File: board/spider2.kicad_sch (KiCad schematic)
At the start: 100 parts, among them J1 NRJ6HH, J10 PJ-320A, J11 PJ359, J12 PJ359, J13 PJ359, J14 PJ359, J15 PJ359, J16 PJ359, J19 PJ359, J2 NRJ6HH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

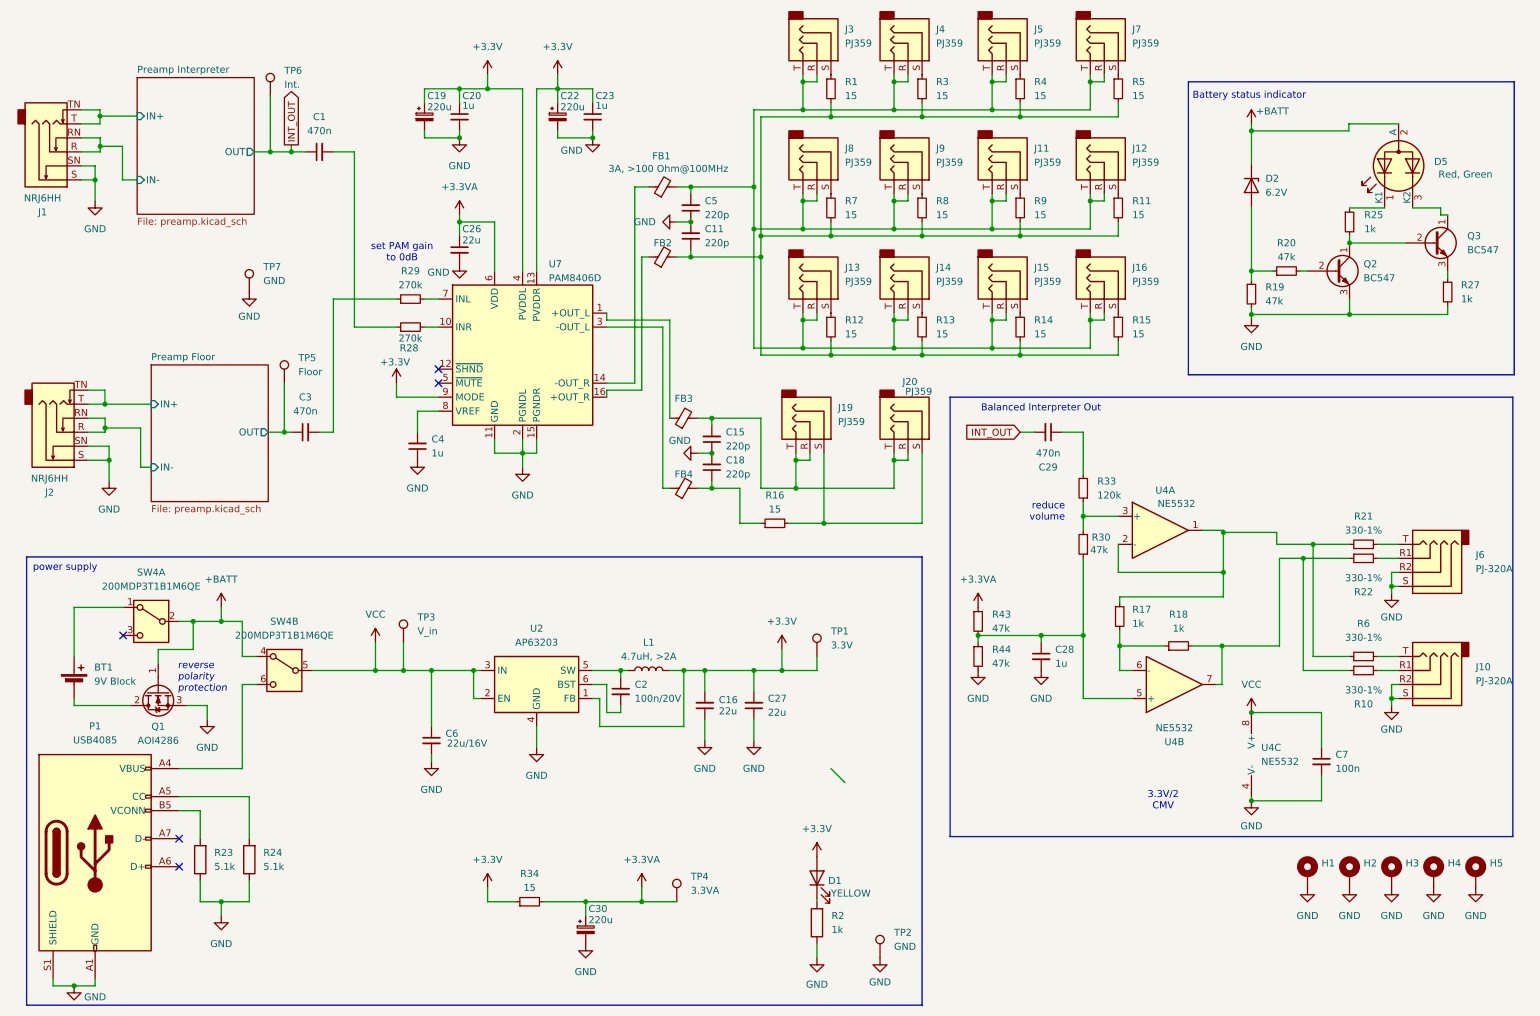
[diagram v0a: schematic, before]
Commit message: silkscreen updates
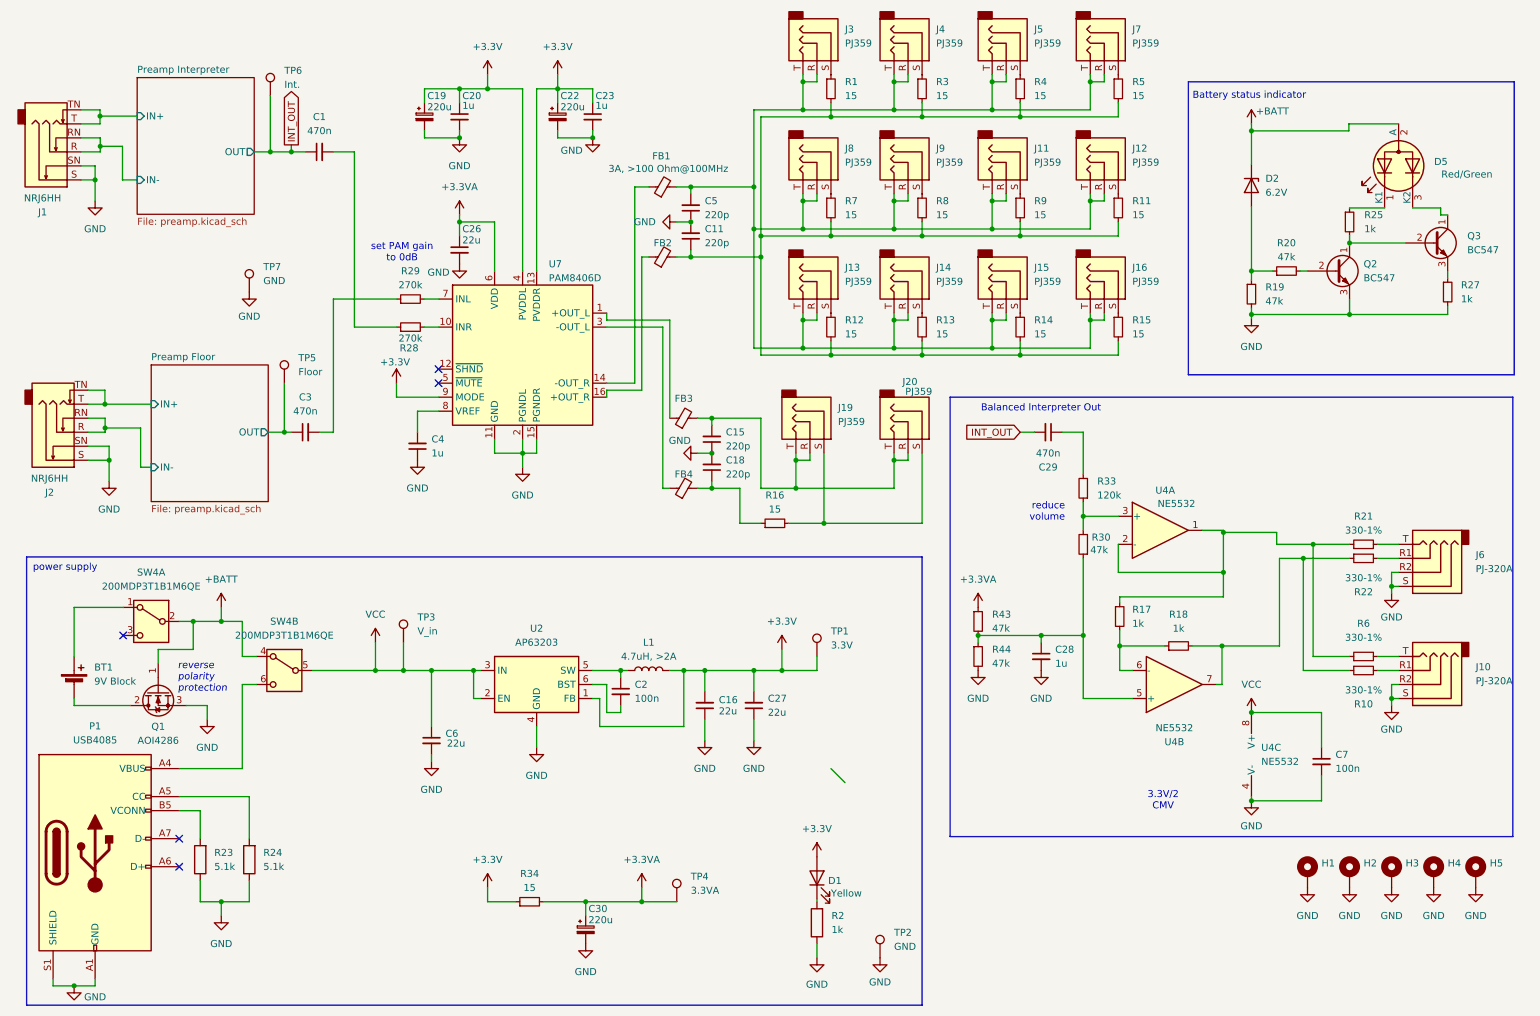
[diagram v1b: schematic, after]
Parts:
- C2: value 100n/20V -> 100n
- C6: value 22u/16V -> 22u
- D1: value YELLOW -> Yellow
- D5: value Red, Green -> Red/Green
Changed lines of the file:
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@@
 			)
 		)
-		(property "Value" "100n/20V"
+		(property "Value" "100n"
 			(at 124.46 139.7062 0)
 			(effects
@@
 			)
 		)
-		(property "Value" "YELLOW"
+		(property "Value" "Yellow"
 			(at 160.02 175.006 90)
 			(effects
@@
 			)
 		)
-		(property "Value" "22u/16V"
+		(property "Value" "22u"
 			(at 90.424 147.828 0)
 			(effects
@@
 			)
 		)
-		(property "Value" "Red, Green"
+		(property "Value" "Red/Green"
 			(at 279.908 44.704 90)
 			(effects

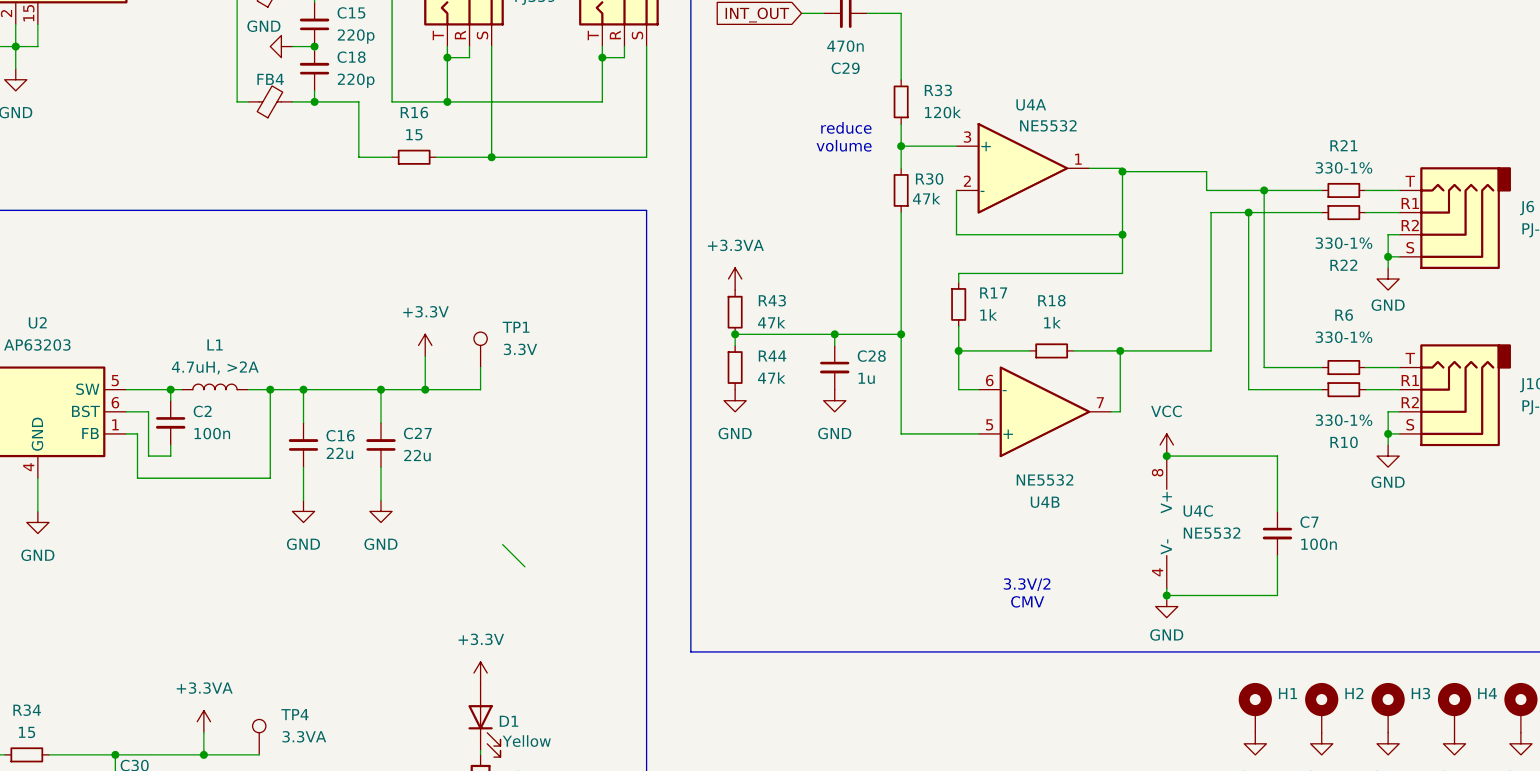
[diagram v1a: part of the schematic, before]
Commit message: correct connector positions, some silkscreen updates
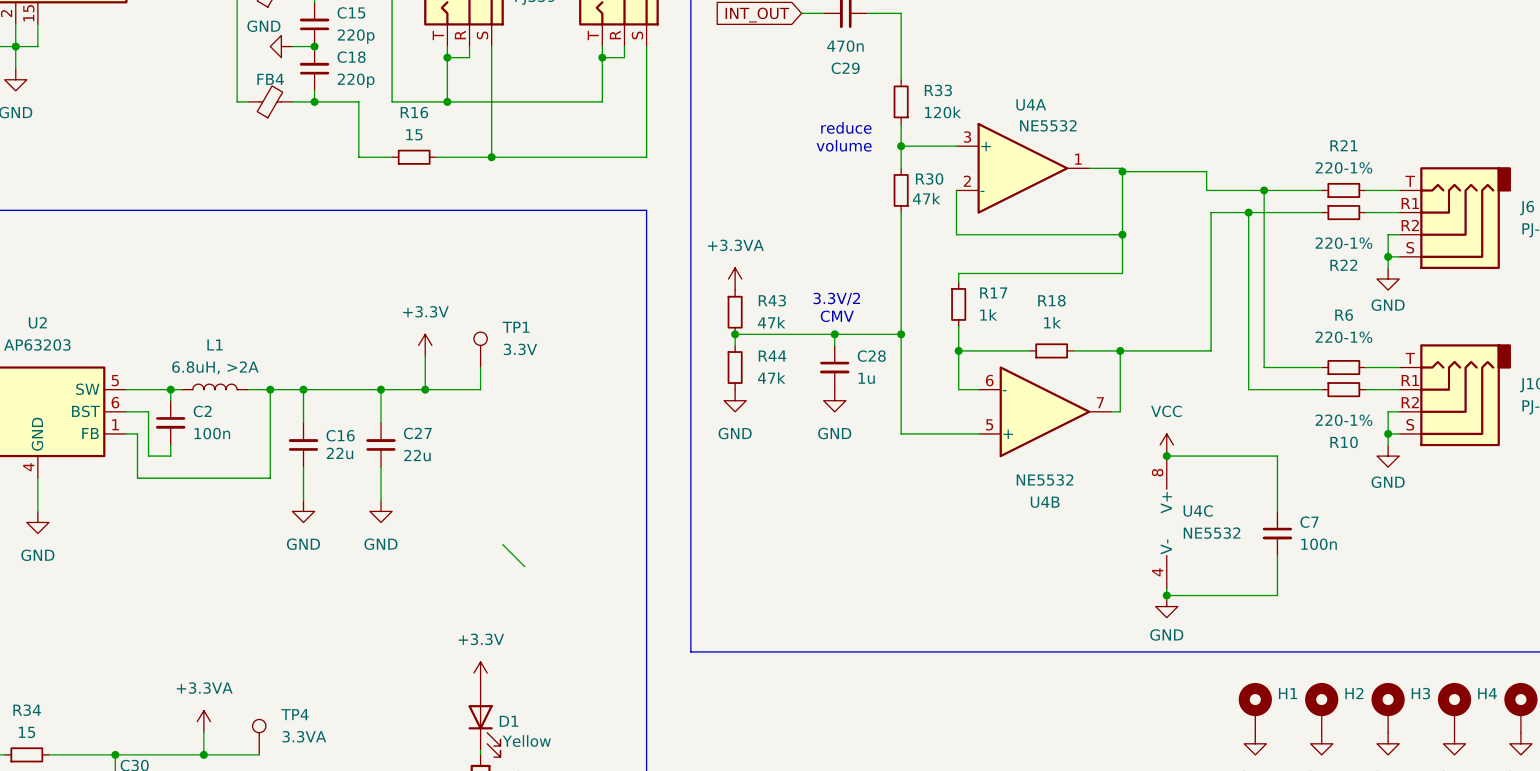
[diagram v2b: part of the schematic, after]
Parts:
- L1: value 4.7uH, >2A -> 6.8uH, >2A
- R10, R21, R22, R6: value 330-1% -> 220-1%
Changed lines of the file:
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@@
 	(text "3.3V/2\nCMV"
 		(exclude_from_sim no)
-		(at 220.218 158.242 0)
+		(at 198.374 125.476 0)
 		(effects
 			(font
@@
 			)
 		)
-		(property "Value" "330-1%"
+		(property "Value" "220-1%"
 			(at 256.54 128.651 90)
 			(effects
@@
 			)
 		)
-		(property "Value" "330-1%"
+		(property "Value" "220-1%"
 			(at 256.54 117.856 90)
 			(effects
@@
 			)
 		)
-		(property "Value" "4.7uH, >2A"
+		(property "Value" "6.8uH, >2A"
 			(at 127 132.08 90)
 			(effects
@@
 			)
 		)
-		(property "Value" "330-1%"
+		(property "Value" "220-1%"
 			(at 256.54 138.176 90)
 			(effects
@@
 			)
 		)
-		(property "Value" "330-1%"
+		(property "Value" "220-1%"
 			(at 256.54 109.22 90)
 			(effects

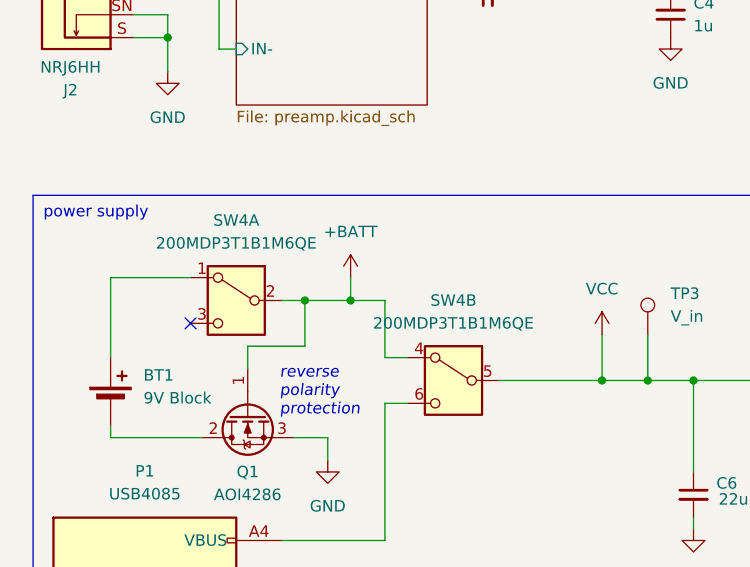
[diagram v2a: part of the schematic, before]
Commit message: EMI improvements, allow PJ358 footprints, DRC fixes, poti changes
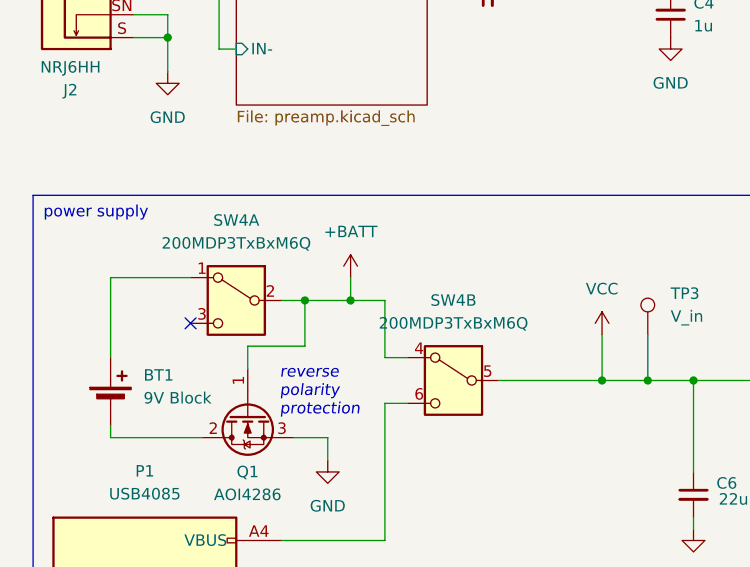
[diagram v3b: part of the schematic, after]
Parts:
- C11, C15, C18, C5: footprint Capacitor_THT:C_Disc_D4.3mm_W1.9mm_P5.00mm -> Capacitor_THT:C_Disc_D3.0mm_W2.0mm_P2.50mm
- J11, J12, J13, J14, J15, J16, J19, J20, J3, J4, J5, J7, J8, J9: footprint custom:Jack_3.5mm_Hybrid_PJ359_20-1655 -> custom:Jack_3.5mm_Hybrid_PJ358_PJ359_20-1655
- SW4: value 200MDP3T1B1M6QE -> 200MDP3TxBxM6Q
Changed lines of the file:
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@@
 			)
 		)
-		(property "Footprint" "custom:Jack_3.5mm_Hybrid_PJ359_20-1655"
+		(property "Footprint" "custom:Jack_3.5mm_Hybrid_PJ358_PJ359_20-1655"
 			(at 157.48 64.77 0)
 			(effects
@@
 			)
 		)
-		(property "Footprint" "custom:Jack_3.5mm_Hybrid_PJ359_20-1655"
+		(property "Footprint" "custom:Jack_3.5mm_Hybrid_PJ358_PJ359_20-1655"
 			(at 157.48 21.59 0)
 			(effects
@@
 			)
 		)
-		(property "Footprint" "Capacitor_THT:C_Disc_D4.3mm_W1.9mm_P5.00mm"
+		(property "Footprint" "Capacitor_THT:C_Disc_D3.0mm_W2.0mm_P2.50mm"
 			(at 138.43 97.79 0)
 			(effects
@@
 			)
 		)
-		(property "Footprint" "custom:Jack_3.5mm_Hybrid_PJ359_20-1655"
+		(property "Footprint" "custom:Jack_3.5mm_Hybrid_PJ358_PJ359_20-1655"
 			(at 209.55 21.59 0)
 			(effects
@@
 			)
 		)
-		(property "Value" "200MDP3T1B1M6QE"
+		(property "Value" "200MDP3TxBxM6Q"
 			(at 36.83 119.38 0)
 			(effects
@@
 			)
 		)
-		(property "Footprint" "custom:Jack_3.5mm_Hybrid_PJ359_20-1655"
+		(property "Footprint" "custom:Jack_3.5mm_Hybrid_PJ358_PJ359_20-1655"
 			(at 191.77 64.77 0)
 			(effects
@@
 			)
 		)
-		(property "Footprint" "Capacitor_THT:C_Disc_D4.3mm_W1.9mm_P5.00mm"
+		(property "Footprint" "Capacitor_THT:C_Disc_D3.0mm_W2.0mm_P2.50mm"
 			(at 134.62 50.8 0)
 			(effects
@@
 			)
 		)
-		(property "Footprint" "Capacitor_THT:C_Disc_D4.3mm_W1.9mm_P5.00mm"
+		(property "Footprint" "Capacitor_THT:C_Disc_D3.0mm_W2.0mm_P2.50mm"
 			(at 134.62 55.88 0)
 			(effects
@@
 			)
 		)
-		(property "Footprint" "custom:Jack_3.5mm_Hybrid_PJ359_20-1655"
+		(property "Footprint" "custom:Jack_3.5mm_Hybrid_PJ358_PJ359_20-1655"
 			(at 156.21 90.17 0)
 			(effects
@@
 			)
 		)
-		(property "Footprint" "custom:Jack_3.5mm_Hybrid_PJ359_20-1655"
+		(property "Footprint" "custom:Jack_3.5mm_Hybrid_PJ358_PJ359_20-1655"
 			(at 191.77 43.18 0)
 			(effects
@@
 			)
 		)
-		(property "Footprint" "custom:Jack_3.5mm_Hybrid_PJ359_20-1655"
+		(property "Footprint" "custom:Jack_3.5mm_Hybrid_PJ358_PJ359_20-1655"
 			(at 173.99 21.59 0)
 			(effects
@@
 			)
 		)
-		(property "Footprint" "Capacitor_THT:C_Disc_D4.3mm_W1.9mm_P5.00mm"
+		(property "Footprint" "Capacitor_THT:C_Disc_D3.0mm_W2.0mm_P2.50mm"
 			(at 138.43 92.71 0)
 			(effects
@@
 			)
 		)
-		(property "Footprint" "custom:Jack_3.5mm_Hybrid_PJ359_20-1655"
+		(property "Footprint" "custom:Jack_3.5mm_Hybrid_PJ358_PJ359_20-1655"
 			(at 209.55 64.77 0)
 			(effects
@@
 			)
 		)
-		(property "Footprint" "custom:Jack_3.5mm_Hybrid_PJ359_20-1655"
+		(property "Footprint" "custom:Jack_3.5mm_Hybrid_PJ358_PJ359_20-1655"
 			(at 173.99 90.17 0)
 			(effects
@@
 			)
 		)
-		(property "Value" "200MDP3T1B1M6QE"
+		(property "Value" "200MDP3TxBxM6Q"
 			(at 60.96 128.27 0)
 			(effects
@@
 			)
 		)
-		(property "Footprint" "custom:Jack_3.5mm_Hybrid_PJ359_20-1655"
+		(property "Footprint" "custom:Jack_3.5mm_Hybrid_PJ358_PJ359_20-1655"
 			(at 209.55 43.18 0)
 			(effects
@@
 			)
 		)
-		(property "Footprint" "custom:Jack_3.5mm_Hybrid_PJ359_20-1655"
+		(property "Footprint" "custom:Jack_3.5mm_Hybrid_PJ358_PJ359_20-1655"
 			(at 173.99 43.18 0)
 			(effects
@@
 			)
 		)
-		(property "Footprint" "custom:Jack_3.5mm_Hybrid_PJ359_20-1655"
+		(property "Footprint" "custom:Jack_3.5mm_Hybrid_PJ358_PJ359_20-1655"
 			(at 191.77 21.59 0)
 			(effects
@@
 			)
 		)
-		(property "Footprint" "custom:Jack_3.5mm_Hybrid_PJ359_20-1655"
+		(property "Footprint" "custom:Jack_3.5mm_Hybrid_PJ358_PJ359_20-1655"
 			(at 157.48 43.18 0)
 			(effects
@@
 			)
 		)
-		(property "Footprint" "custom:Jack_3.5mm_Hybrid_PJ359_20-1655"
+		(property "Footprint" "custom:Jack_3.5mm_Hybrid_PJ358_PJ359_20-1655"
 			(at 173.99 64.77 0)
 			(effects
